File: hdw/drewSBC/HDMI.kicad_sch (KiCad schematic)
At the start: 3 parts

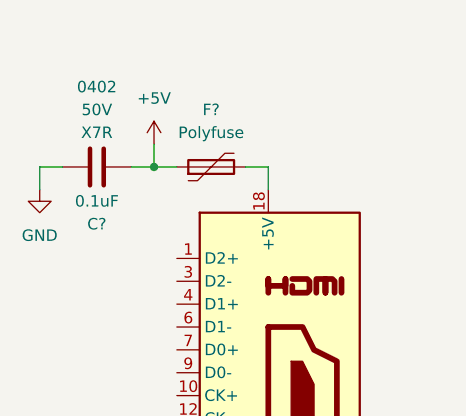
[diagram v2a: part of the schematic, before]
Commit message: ripped up ETH phy
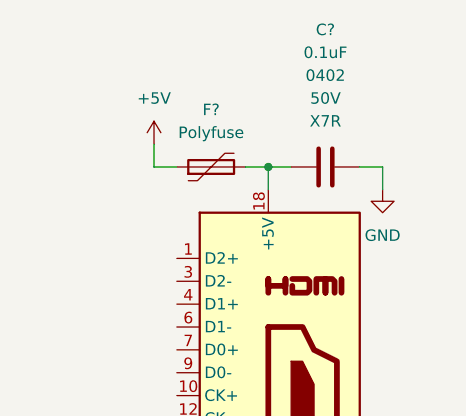
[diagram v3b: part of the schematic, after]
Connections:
- net +5V: no longer C?.2
- net GND: now also C?.2; no longer C?.1
- net at F?.2, J?.18 (+5V): now also C?.1
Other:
- moved on the sheet: C?
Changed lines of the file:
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@@
     (company "Drew Maatman")
   )
-  (junction (at 231.14 57.15) (diameter 0) (color 0 0 0 0)
+  (junction (at 243.84 57.15) (diameter 0) (color 0 0 0 0)
   )
   (wire (pts (xy 243.84 57.15) (xy 243.84 59.69))
@@
     (stroke (width 0) (type default) (color 0 0 0 0))
   )
-  (wire (pts (xy 228.6 57.15) (xy 231.14 57.15))
-    (stroke (width 0) (type default) (color 0 0 0 0))
-  )
-  (wire (pts (xy 218.44 57.15) (xy 220.98 57.15))
-    (stroke (width 0) (type default) (color 0 0 0 0))
-  )
-  (wire (pts (xy 218.44 59.69) (xy 218.44 57.15))
+  (wire (pts (xy 243.84 57.15) (xy 246.38 57.15))
     (stroke (width 0) (type default) (color 0 0 0 0))
   )
@@
     (stroke (width 0) (type default) (color 0 0 0 0))
   )
+  (wire (pts (xy 256.54 57.15) (xy 254 57.15))
+    (stroke (width 0) (type default) (color 0 0 0 0))
+  )
+  (wire (pts (xy 256.54 59.69) (xy 256.54 57.15))
+    (stroke (width 0) (type default) (color 0 0 0 0))
+  )
   (wire (pts (xy 241.3 57.15) (xy 243.84 57.15))
     (stroke (width 0) (type default) (color 0 0 0 0))
   )
-  (symbol (lib_id "power:GND") (at 218.44 59.69 0) (unit 1)
+  (symbol (lib_id "power:GND") (at 256.54 59.69 0) (unit 1)
     (in_bom yes) (on_board yes) (fields_autoplaced)
-    (property "Reference" "#PWR?" (id 0) (at 218.44 66.04 0)
+    (property "Reference" "#PWR?" (id 0) (at 256.54 66.04 0)
       (effects (font (size 1.27 1.27)) hide)
     )
-    (property "Value" "GND" (id 1) (at 218.44 64.77 0))
-    (property "Footprint" "" (id 2) (at 218.44 59.69 0)
+    (property "Value" "GND" (id 1) (at 256.54 64.77 0))
+    (property "Footprint" "" (id 2) (at 256.54 59.69 0)
       (effects (font (size 1.27 1.27)) hide)
     )
-    (property "Datasheet" "" (id 3) (at 218.44 59.69 0)
+    (property "Datasheet" "" (id 3) (at 256.54 59.69 0)
       (effects (font (size 1.27 1.27)) hide)
     )
@@
     (pin "2")
   )
-  (symbol (lib_id "Custom_Library:C_Custom") (at 224.79 57.15 90) (unit 1)
-    (in_bom yes) (on_board yes)
-    (property "Reference" "C?" (id 0) (at 224.79 63.5 90))
-    (property "Value" "0.1uF" (id 1) (at 224.79 60.96 90))
-    (property "Footprint" "Capacitors_SMD:C_0402" (id 2) (at 228.6 56.1848 0)
+  (symbol (lib_id "Custom_Library:C_Custom") (at 250.19 57.15 90) (unit 1)
+    (in_bom yes) (on_board yes) (fields_autoplaced)
+    (property "Reference" "C?" (id 0) (at 250.19 41.91 90))
+    (property "Value" "0.1uF" (id 1) (at 250.19 44.45 90))
+    (property "Footprint" "Capacitors_SMD:C_0402" (id 2) (at 254 56.1848 0)
       (effects (font (size 1.27 1.27)) hide)
     )
-    (property "Datasheet" "" (id 3) (at 222.25 56.515 0)
+    (property "Datasheet" "" (id 3) (at 247.65 56.515 0)
       (effects (font (size 1.27 1.27)) hide)
     )
-    (property "display_footprint" "0402" (id 4) (at 224.79 48.26 90))
-    (property "Voltage" "50V" (id 5) (at 224.79 50.8 90))
-    (property "Dielectric" "X7R" (id 6) (at 224.79 53.34 90))
-    (property "Digi-Key PN" "490-10698-1-ND" (id 7) (at 212.09 46.355 0)
+    (property "display_footprint" "0402" (id 4) (at 250.19 46.99 90))
+    (property "Voltage" "50V" (id 5) (at 250.19 49.53 90))
+    (property "Dielectric" "X7R" (id 6) (at 250.19 52.07 90))
+    (property "Digi-Key PN" "490-10698-1-ND" (id 7) (at 237.49 46.355 0)
       (effects (font (size 1.524 1.524)) hide)
     )

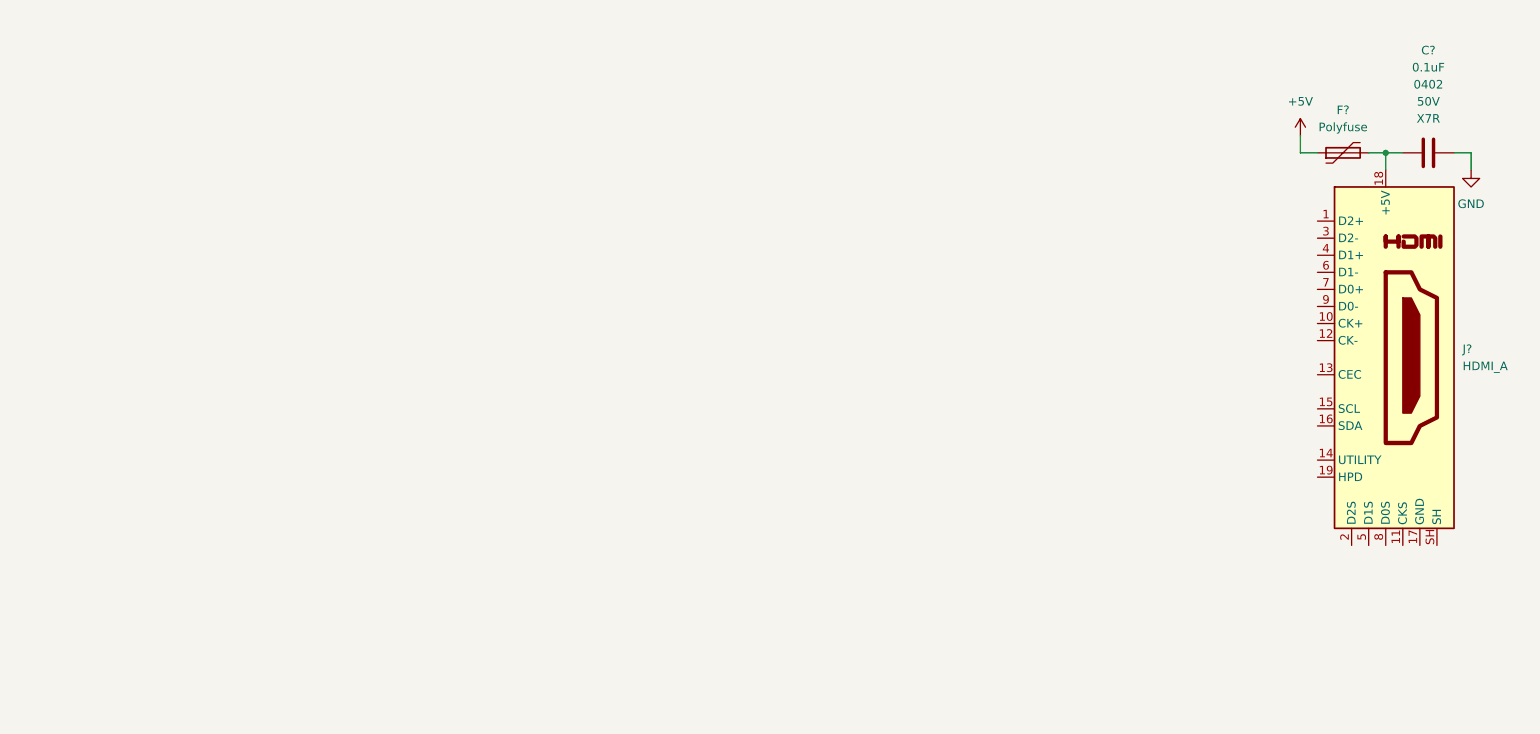
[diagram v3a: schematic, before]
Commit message: rebuilt HDMI sheet
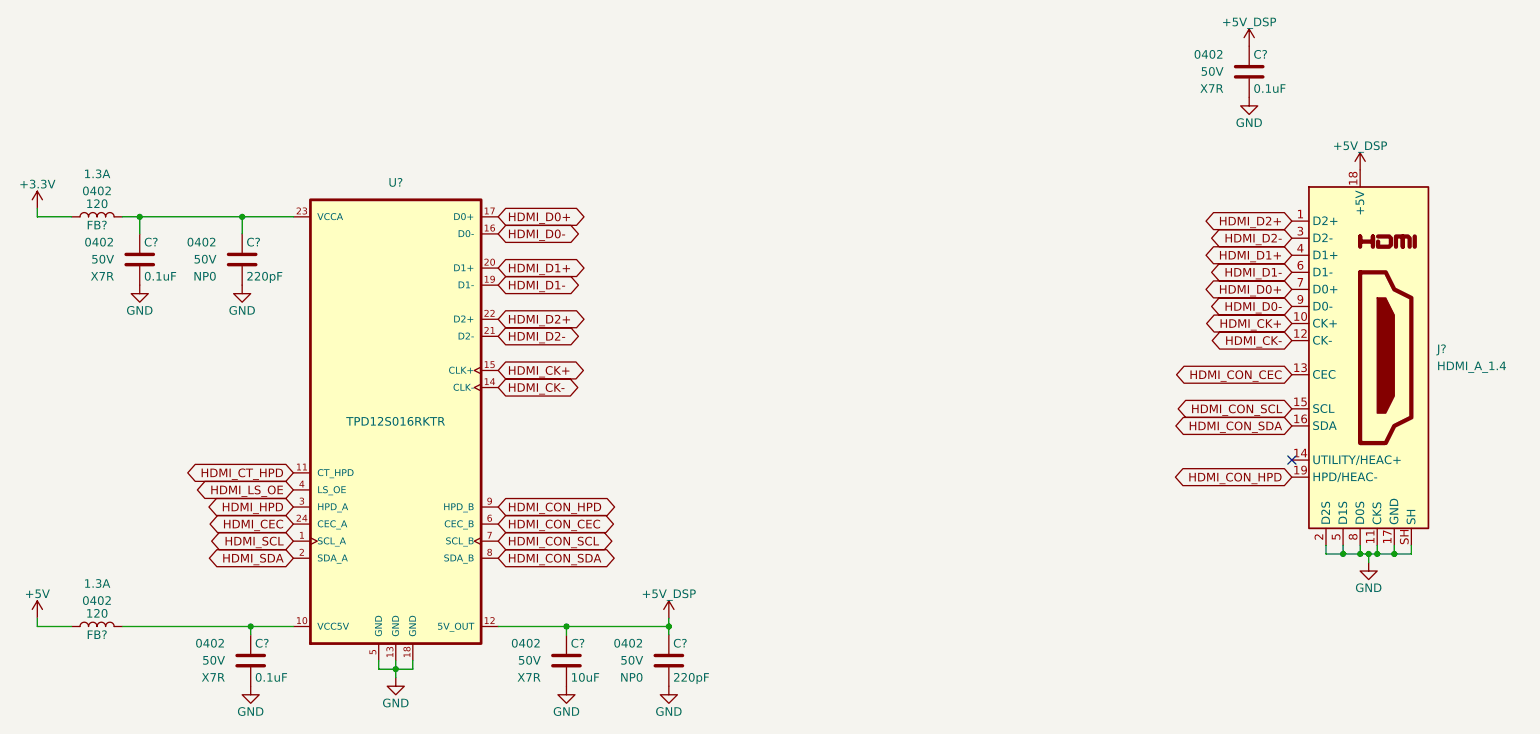
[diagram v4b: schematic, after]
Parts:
- removed C?: 0.1uF, Capacitors_SMD:C_0402, symbol Custom_Library:C_Custom
- removed F?: Polyfuse, symbol Device:Polyfuse
- removed J?: HDMI_A, symbol Connector:HDMI_A
- added C?: 10uF, Capacitors_SMD:C_0402, symbol Custom_Library:C_Custom
- added C? (x3): 0.1uF, Capacitors_SMD:C_0402, symbol Custom_Library:C_Custom
- added C? (x2): 220pF, Capacitors_SMD:C_0402, symbol Custom_Library:C_Custom
- added FB? (x2): 120, symbol Custom Library:FB_Custom
- added J?: HDMI_A_1.4, symbol Connector:HDMI_A_1.4
- added U?: TPD12S016RKTR, Custom Footprints Library:IC_TPD12S016RKTR, symbol Custom Library:TPD12S016RKTR
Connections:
- net +5V: now also FB?.1
- net GND: now also C?.2, C?.2, C?.2, C?.2, C?.2, C?.2, J?.11 (CKS), J?.17 (GND), J?.2 (D2S), J?.5 (D1S), J?.8 (D0S), J?.SH, U?.13 (GND), U?.18 (GND), U?.5 (GND)
- new net: C?.1, C?.1, FB?.2, U?.23 (VCCA)
- new net: C?.1, FB?.2, U?.10 (VCC5V)
- new net +3.3V: FB?.1
- new net +5V_DSP: C?.1, C?.1, C?.1, J?.18 (+5V), U?.12 (5V_OUT)
- new net HDMI_CEC: U?.24 (CEC_A)
- new net HDMI_CK+: J?.10 (CK+), U?.15 (CLK+)
- new net HDMI_CK-: J?.12 (CK-), U?.14 (CLK-)
- new net HDMI_CON_CEC: J?.13 (CEC), U?.6 (CEC_B)
- new net HDMI_CON_HPD: J?.19 (HPD/HEAC-), U?.9 (HPD_B)
- new net HDMI_CON_SCL: J?.15 (SCL), U?.7 (SCL_B)
- new net HDMI_CON_SDA: J?.16 (SDA), U?.8 (SDA_B)
- new net HDMI_CT_HPD: U?.11 (CT_HPD)
- new net HDMI_D0+: J?.7 (D0+), U?.17 (D0+)
- new net HDMI_D0-: J?.9 (D0-), U?.16 (D0-)
- new net HDMI_D1+: J?.4 (D1+), U?.20 (D1+)
- new net HDMI_D1-: J?.6 (D1-), U?.19 (D1-)
- new net HDMI_D2+: J?.1 (D2+), U?.22 (D2+)
- new net HDMI_D2-: J?.3 (D2-), U?.21 (D2-)
- new net HDMI_HPD: U?.3 (HPD_A)
- new net HDMI_LS_OE: U?.4 (LS_OE)
- new net HDMI_SCL: U?.1 (SCL_A)
- new net HDMI_SDA: U?.2 (SDA_A)
- no-connect marks 0 -> 1
